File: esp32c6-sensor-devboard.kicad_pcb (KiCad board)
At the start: 4 copper layers, 183 parts, among them J1 Conn_01x04_Pin, J2 Micro_SD_Card_Det1, J3 Screw_Terminal_01x02, J4 USB_C_Receptacle_USB2.0_14P, J5 Screw_Terminal_01x02, J6 Screw_Terminal_01x06, J7 Screw_Terminal_01x04, J8 Conn_01x04_Pin, J9 Conn_01x03_Pin, SW1 SW_Push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

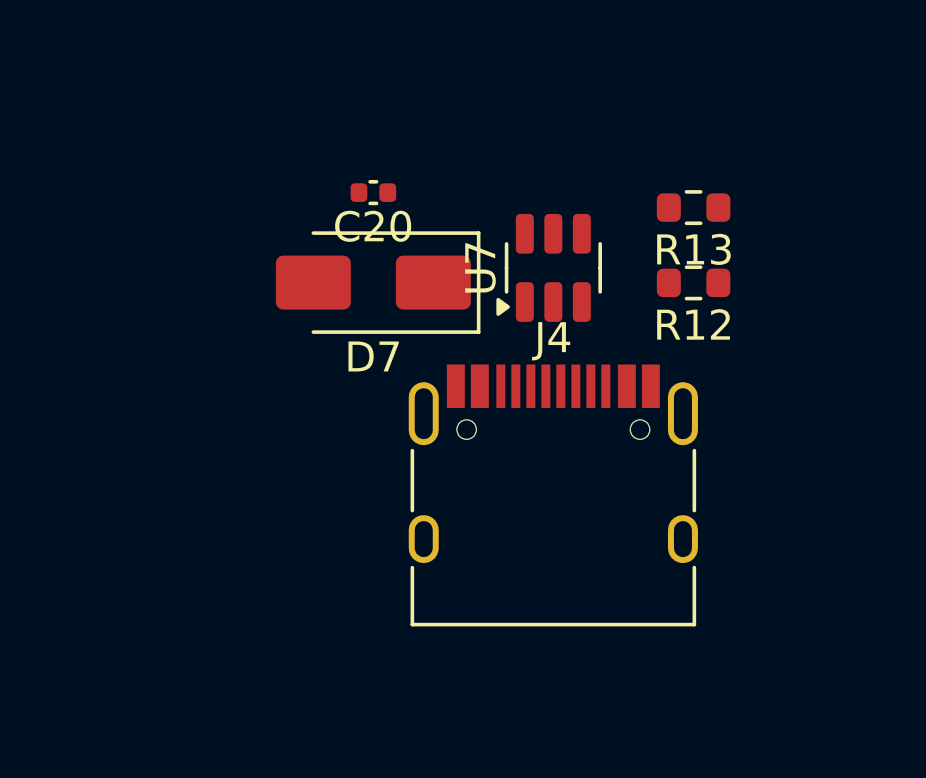
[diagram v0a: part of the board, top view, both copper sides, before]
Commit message: pcb: usb connector layout
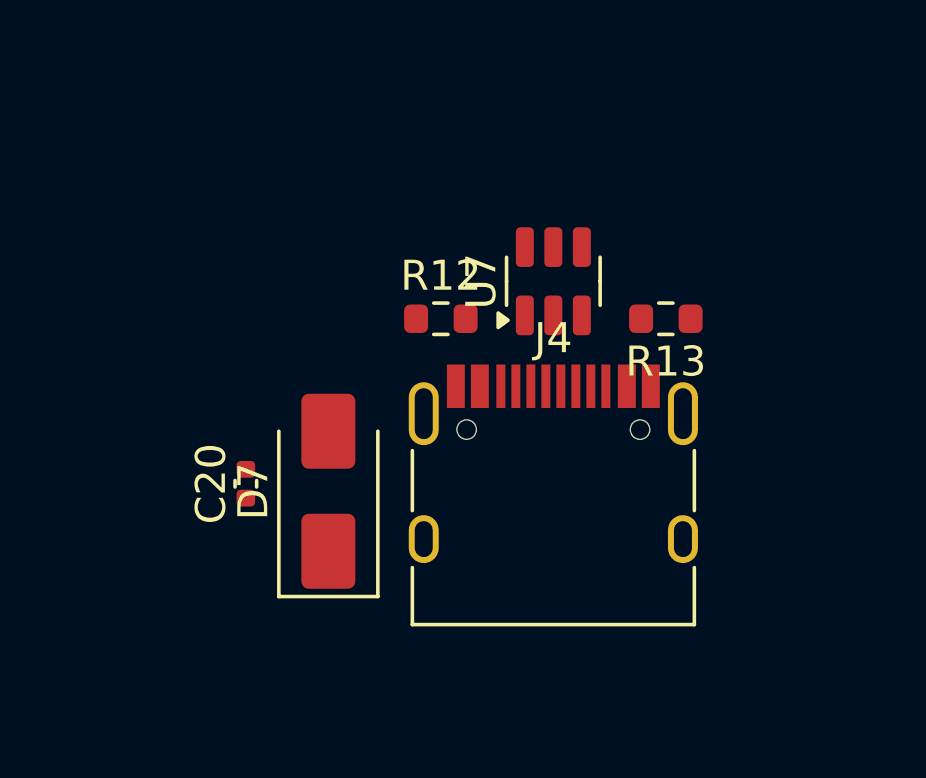
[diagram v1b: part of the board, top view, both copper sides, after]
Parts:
- moved C20 10.6 mm to (140.5, 124.2), turned to 90 degrees
- moved R12 8.51 mm to (147.0, 118.8), turned to 0 degrees
- moved D7 7.11 mm to (143.2, 124.5), turned to 90 degrees
- moved R13 3.82 mm to (154.5, 118.8)
- moved U7 0.44 mm to (150.8, 117.5)

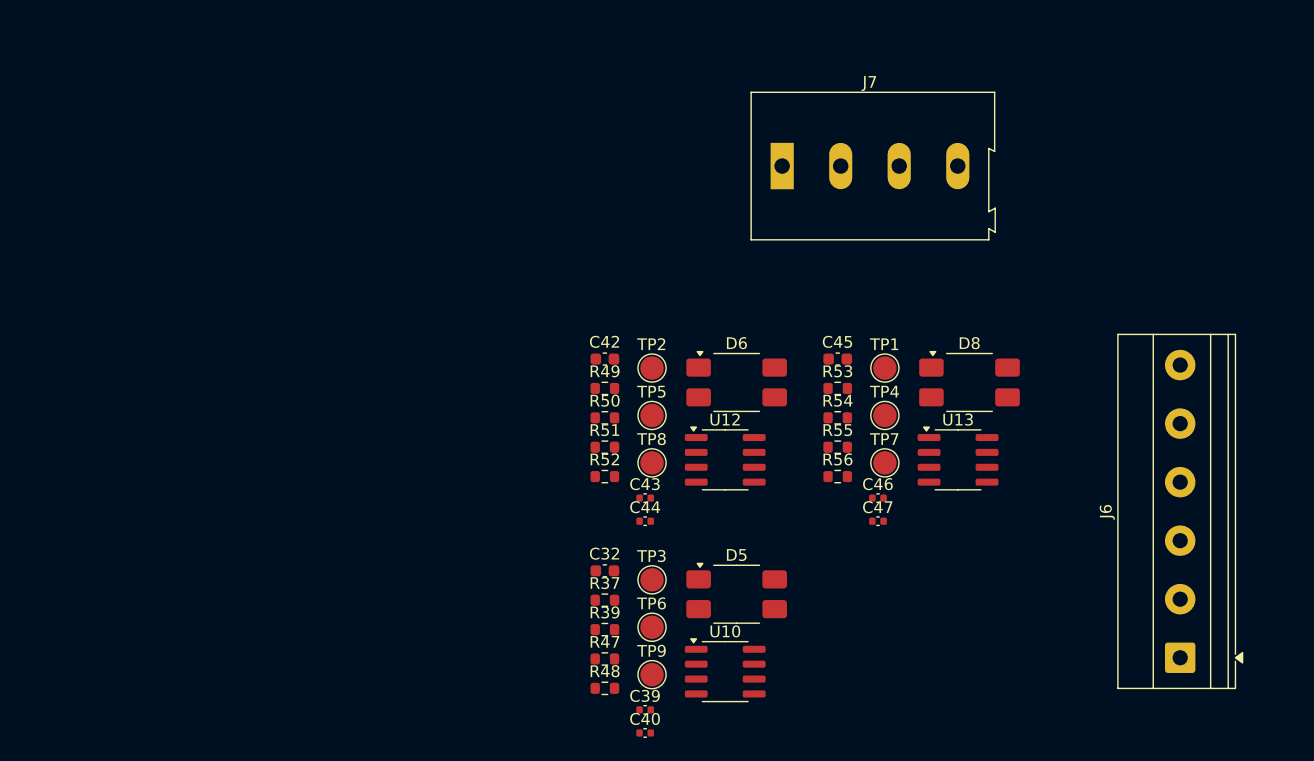
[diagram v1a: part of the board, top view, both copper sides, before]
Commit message: pcb: ac level shifter layout
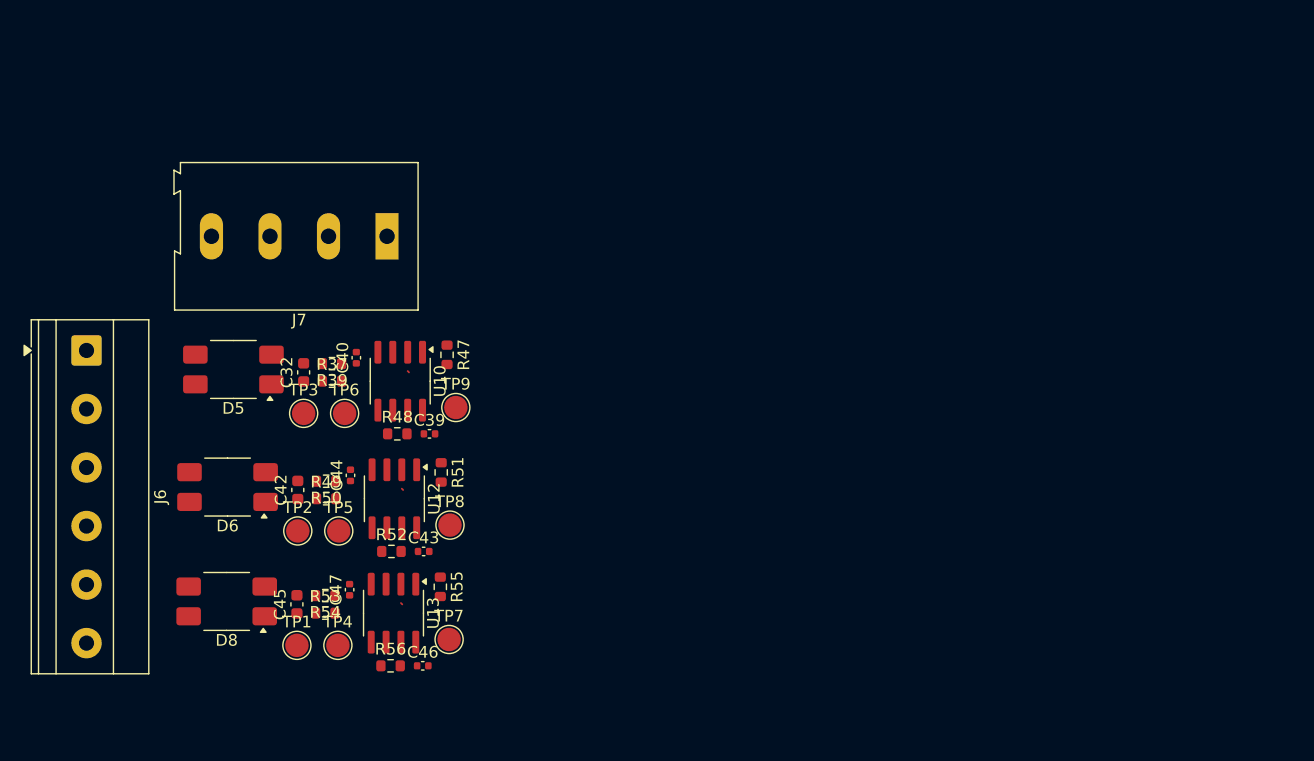
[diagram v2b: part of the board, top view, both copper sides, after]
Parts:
- moved J6 97.0 mm to (19.6, 147.8), turned to -90 degrees
- moved D8 66.1 mm to (31.6, 169.2), turned to 180 degrees
- moved TP1 55.5 mm to (37.5, 172.9)
- moved C45 50.7 mm to (37.5, 169.4), turned to 90 degrees
- moved TP4 50.7 mm to (41.0, 172.9)
- moved U13 50.0 mm to (45.8, 170.2), turned to -90 degrees
- moved R53 47.8 mm to (40.0, 170.2)
- moved D5 47.1 mm to (32.1, 149.4), turned to 180 degrees
- moved R54 46.3 mm to (40.0, 168.7), turned to 180 degrees
- moved C47 45.5 mm to (42.0, 168.2), turned to 90 degrees
- moved D6 44.4 mm to (31.6, 159.4), turned to 180 degrees
- moved R56 41.5 mm to (45.5, 174.7)
- moved C46 41.4 mm to (48.3, 174.7)
- moved C40 40.4 mm to (42.6, 148.4), turned to 90 degrees
- moved TP7 40.2 mm to (50.5, 172.4)
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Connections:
- D5 pad 3: /AC Level Shifter2/I1 -> /AC Level Shifter2/I2
- D5 pad 4: /AC Level Shifter2/I2 -> /AC Level Shifter2/I1
- D6 pad 3: /AC Level Shifter1/I1 -> /AC Level Shifter1/I2
- D6 pad 4: /AC Level Shifter1/I2 -> /AC Level Shifter1/I1
- D8 pad 3: /AC Level Shifter/I1 -> /AC Level Shifter/I2
- D8 pad 4: /AC Level Shifter/I2 -> /AC Level Shifter/I1

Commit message: pcb: rf layout
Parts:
- moved C52 5.26 mm to (138.7, 85.2)
- moved R11 4.83 mm to (141.6, 97.9), turned to -45 degrees
- moved L4 4.61 mm to (145.0, 90.2), turned to -45 degrees
- moved C29 4.37 mm to (143.8, 89.5), turned to -135 degrees
- moved L6 4.26 mm to (135.7, 85.2), turned to 0 degrees
- moved L7 4.25 mm to (137.2, 85.8), turned to 90 degrees
- moved C28 4.12 mm to (145.0, 91.8), turned to 180 degrees
- moved AE1 3.75 mm to (132.2, 85.5)
- moved C27 3.69 mm to (145.0, 98.1), turned to 45 degrees
- moved Y2 3.51 mm to (143.0, 96.5), turned to 135 degrees
- moved C11 2.05 mm to (145.0, 93.2)
- moved C9 1.74 mm to (140.8, 90.3)
- moved C8 1.74 mm to (139.8, 90.2)
- moved C26 1.42 mm to (141.1, 94.6), turned to 45 degrees
- moved C10 0.57 mm to (142.5, 91.8), turned to 180 degrees
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
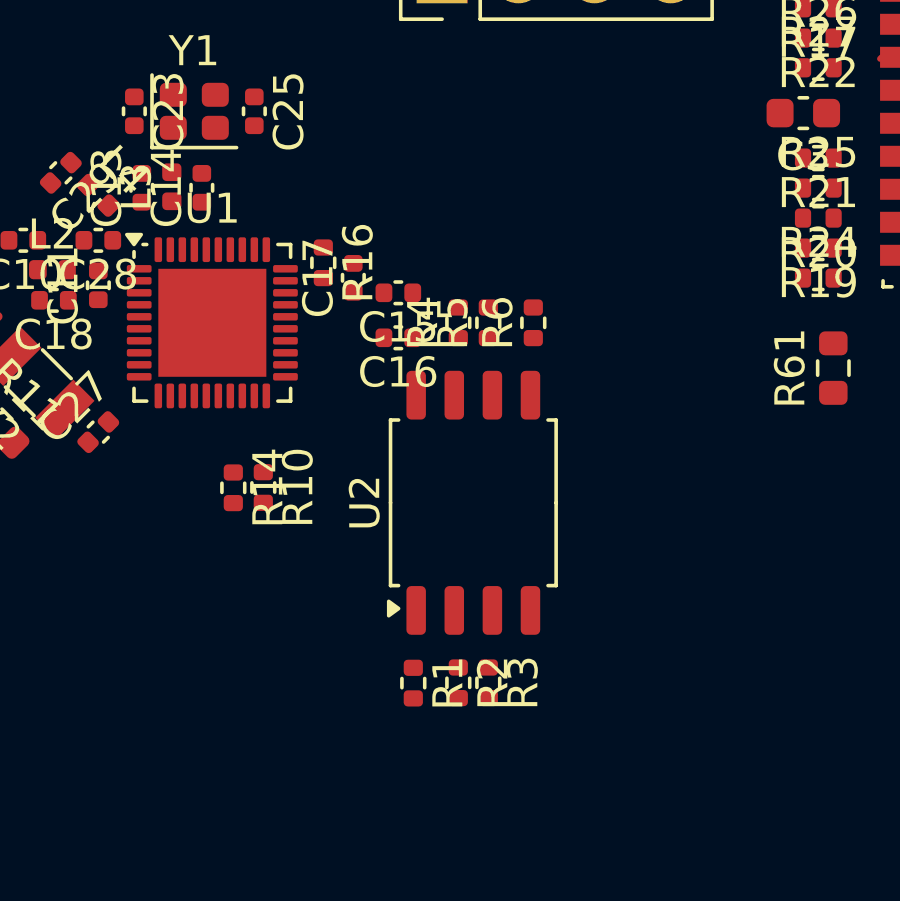
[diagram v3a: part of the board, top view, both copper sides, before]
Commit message: pcb: spi flash layout
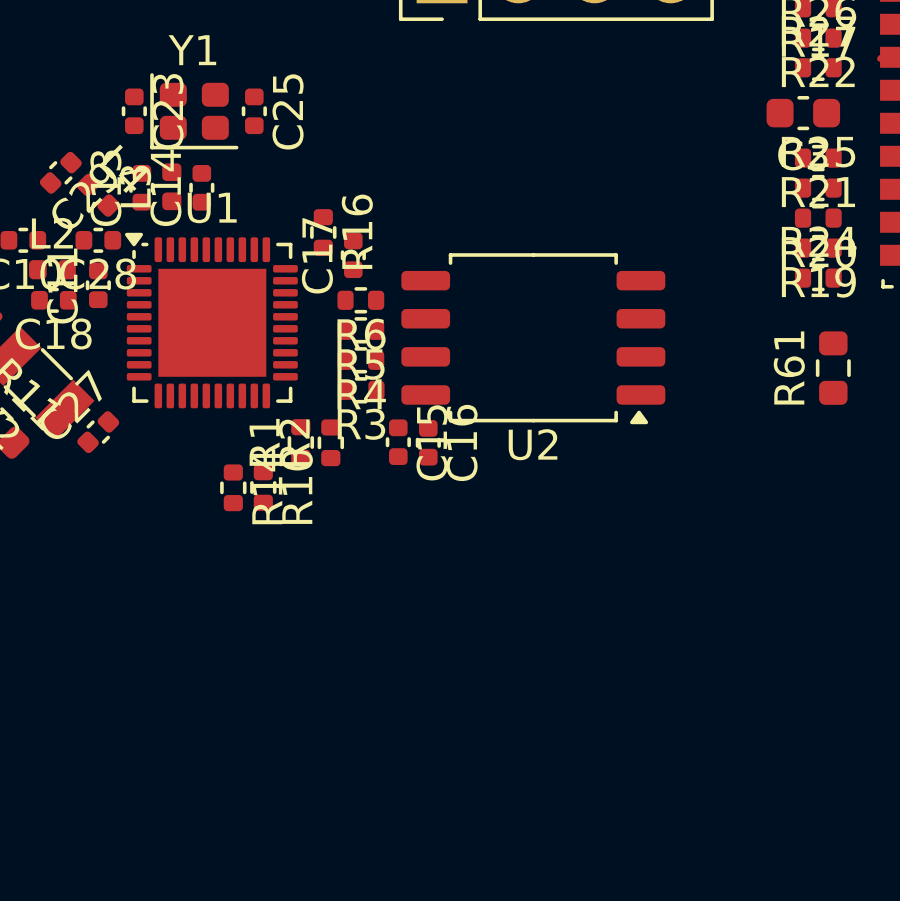
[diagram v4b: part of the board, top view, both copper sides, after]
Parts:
- moved R3 10.6 mm to (153.8, 96.8), turned to 180 degrees
- moved R2 9.06 mm to (152.8, 98.5), turned to 90 degrees
- moved R1 8.85 mm to (151.8, 98.5), turned to 90 degrees
- moved U2 5.85 mm to (159.5, 95.0), turned to 180 degrees
- moved R6 5.80 mm to (153.8, 93.8), turned to 180 degrees
- moved C15 4.98 mm to (155.0, 98.5), turned to -90 degrees
- moved R5 4.26 mm to (153.8, 94.8), turned to 180 degrees
- moved C16 3.64 mm to (156.0, 98.5), turned to -90 degrees
- moved R4 3.48 mm to (153.8, 95.8), turned to 180 degrees
- moved R16 1.01 mm to (152.5, 91.5)
- moved C17 0.75 mm to (153.5, 92.2)

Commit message: pcb: fix 3v3 ldo layout
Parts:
- moved JP3 91.1 mm to (230.0, 26.2), turned to -90 degrees
- moved J1 7.65 mm to (149.9, 79.0)
- moved JP1 7.19 mm to (174.8, 74.5), turned to -90 degrees
- moved C1 3.72 mm to (224.2, 32.8)
- moved C2 3.72 mm to (230.2, 32.2)
- moved D2 3.72 mm to (222.5, 29.5)
- moved R15 3.72 mm to (224.2, 29.5)
- moved TP17 3.72 mm to (227.2, 33.8)
- moved U3 3.72 mm to (227.2, 30.2)
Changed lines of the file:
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@@
 	(footprint "Connector_PinHeader_2.54mm:PinHeader_1x04_P2.54mm_Vertical"
 		(layer "F.Cu")
-		(at 156.46 83 90)
+		(at 149.94 79 90)
 		(descr "Through hole straight pin header, 1x04, 2.54mm pitch, single row")
 		(tags "Through hole pin header THT 1x04 2.54mm single row")
@@
 	(footprint "Capacitor_SMD:C_0603_1608Metric"
 		(layer "F.Cu")
-		(at 223.8625 29.075 -90)
+		(at 224.25 32.775 -90)
 		(descr "Capacitor SMD 0603 (1608 Metric), square (rectangular) end terminal, IPC-7351 nominal, (Body size source: IPC-SM-782 page 76, https://www.pcb-3d.com/wordpress/wp-content/uploads/ipc-sm-782a_amendment_1_and_2.pdf), generated with kicad-footprint-generator")
 		(tags "capacitor")
@@
 	(footprint "Capacitor_SMD:C_0603_1608Metric"
 		(layer "F.Cu")
-		(at 229.8625 28.55 -90)
+		(at 230.25 32.25 -90)
 		(descr "Capacitor SMD 0603 (1608 Metric), square (rectangular) end terminal, IPC-7351 nominal, (Body size source: IPC-SM-782 page 76, https://www.pcb-3d.com/wordpress/wp-content/uploads/ipc-sm-782a_amendment_1_and_2.pdf), generated with kicad-footprint-generator")
 		(tags "capacitor")
@@
 	(footprint "Connector_PinHeader_2.54mm:PinHeader_1x02_P2.54mm_Vertical"
 		(layer "F.Cu")
-		(at 225.49 117.195)
+		(at 230.025 26.25 -90)
 		(descr "Through hole straight pin header, 1x02, 2.54mm pitch, single row")
 		(tags "Through hole pin header THT 1x02 2.54mm single row")
 		(property "Reference" "JP3"
-			(at 0 -2.38 0)
+			(at 0 -2.38 90)
 			(layer "F.SilkS")
 			(effects
@@
 		)
 		(property "Value" "Jumper_2_Bridged"
-			(at 0 4.92 0)
+			(at 0 4.92 90)
 			(layer "F.Fab")
 			(effects
@@
 		)
 		(property "Datasheet" "~"
-			(at 0 0 0)
+			(at 0 0 90)
 			(layer "F.Fab")
 			(hide yes)
@@
 		)
 		(property "Description" "Jumper, 2-pole, closed/bridged"
-			(at 0 0 0)
+			(at 0 0 90)
 			(layer "F.Fab")
 			(hide yes)
@@
 		(attr through_hole exclude_from_bom)
 		(fp_line
-			(start -1.38 -1.38)
-			(end 0 -1.38)
+			(start -1.38 3.92)
+			(end 1.38 3.92)
 			(stroke
 				(width 0.12)
@@
 		)
 		(fp_line
-			(start -1.38 0)
-			(end -1.38 -1.38)
+			(start -1.38 1.27)
+			(end -1.38 3.92)
 			(stroke
 				(width 0.12)
@@
 		(fp_line
 			(start -1.38 1.27)
-			(end -1.38 3.92)
+			(end 1.38 1.27)
 			(stroke
 				(width 0.12)
@@
 		)
 		(fp_line
-			(start -1.38 1.27)
-			(end 1.38 1.27)
+			(start 1.38 1.27)
+			(end 1.38 3.92)
 			(stroke
 				(width 0.12)
@@
 		)
 		(fp_line
-			(start -1.38 3.92)
-			(end 1.38 3.92)
+			(start -1.38 0)
+			(end -1.38 -1.38)
 			(stroke
 				(width 0.12)
@@
 		)
 		(fp_line
-			(start 1.38 1.27)
-			(end 1.38 3.92)
+			(start -1.38 -1.38)
+			(end 0 -1.38)
 			(stroke
 				(width 0.12)
@@
 		)
 		(fp_line
-			(start -1.77 -1.77)
-			(end -1.77 4.32)
+			(start -1.77 4.32)
+			(end 1.77 4.32)
 			(stroke
 				(width 0.05)
@@
 		)
 		(fp_line
-			(start -1.77 4.32)
-			(end 1.77 4.32)
+			(start 1.77 4.32)
+			(end 1.77 -1.77)
 			(stroke
 				(width 0.05)
@@
 		)
 		(fp_line
-			(start 1.77 -1.77)
-			(end -1.77 -1.77)
+			(start -1.77 -1.77)
+			(end -1.77 4.32)
 			(stroke
 				(width 0.05)
@@
 		)
 		(fp_line
-			(start 1.77 4.32)
-			(end 1.77 -1.77)
+			(start 1.77 -1.77)
+			(end -1.77 -1.77)
 			(stroke
 				(width 0.05)
@@
 		)
 		(fp_line
-			(start -1.27 -0.635)
-			(end -0.635 -1.27)
+			(start -1.27 3.81)
+			(end -1.27 -0.635)
 			(stroke
 				(width 0.1)
@@
 		)
 		(fp_line
-			(start -1.27 3.81)
-			(end -1.27 -0.635)
+			(start 1.27 3.81)
+			(end -1.27 3.81)
 			(stroke
 				(width 0.1)
@@
 		)
 		(fp_line
-			(start -0.635 -1.27)
-			(end 1.27 -1.27)
+			(start -1.27 -0.635)
+			(end -0.635 -1.27)
 			(stroke
 				(width 0.1)
@@
 		)
 		(fp_line
-			(start 1.27 -1.27)
-			(end 1.27 3.81)
+			(start -0.635 -1.27)
+			(end 1.27 -1.27)
 			(stroke
 				(width 0.1)
@@
 		)
 		(fp_line
-			(start 1.27 3.81)
-			(end -1.27 3.81)
+			(start 1.27 -1.27)
+			(end 1.27 3.81)
 			(stroke
 				(width 0.1)
@@
 		)
 		(fp_text user "${REFERENCE}"
-			(at 0 1.27 90)
+			(at 0 1.27 0)
 			(layer "F.Fab")
 			(effects
@@
 		)
 		(pad "1" thru_hole rect
-			(at 0 0)
+			(at 0 0 270)
 			(size 1.7 1.7)
 			(drill 1)
@@
 		)
 		(pad "2" thru_hole circle
-			(at 0 2.54)
+			(at 0 2.54 270)
 			(size 1.7 1.7)
 			(drill 1)
@@
 	(footprint "Package_TO_SOT_SMD:SOT-23-5"
 		(layer "F.Cu")
-		(at 226.8625 26.55 180)
+		(at 227.25 30.25 180)
 		(descr "SOT, 5 Pin (JEDEC MO-178 Var AA https://www.jedec.org/document_search?search_api_views_fulltext=MO-178), generated with kicad-footprint-generator ipc_gullwing_generator.py")
 		(tags "SOT TO_SOT_SMD")
@@
 	(footprint "Connector_PinHeader_2.54mm:PinHeader_1x02_P2.54mm_Vertical"
 		(layer "F.Cu")
-		(at 181.8975 73.68 90)
+		(at 174.75 74.5 -90)
 		(descr "Through hole straight pin header, 1x02, 2.54mm pitch, single row")
 		(tags "Through hole pin header THT 1x02 2.54mm single row")
@@
 		(attr through_hole exclude_from_bom)
 		(fp_line
-			(start -1.38 -1.38)
-			(end 0 -1.38)
+			(start -1.38 3.92)
+			(end 1.38 3.92)
 			(stroke
 				(width 0.12)
@@
 		)
 		(fp_line
-			(start -1.38 0)
-			(end -1.38 -1.38)
+			(start -1.38 1.27)
+			(end -1.38 3.92)
 			(stroke
 				(width 0.12)
@@
 		)
 		(fp_line
-			(start 1.38 1.27)
-			(end 1.38 3.92)
+			(start -1.38 1.27)
+			(end 1.38 1.27)
 			(stroke
 				(width 0.12)
@@
 		)
 		(fp_line
-			(start -1.38 1.27)
-			(end 1.38 1.27)
+			(start 1.38 1.27)
+			(end 1.38 3.92)
 			(stroke
 				(width 0.12)
@@
 		)
 		(fp_line
-			(start -1.38 1.27)
-			(end -1.38 3.92)
+			(start -1.38 0)
+			(end -1.38 -1.38)
 			(stroke
 				(width 0.12)
@@
 		)
 		(fp_line
-			(start -1.38 3.92)
-			(end 1.38 3.92)
+			(start -1.38 -1.38)
+			(end 0 -1.38)
 			(stroke
 				(width 0.12)
@@
 		)
 		(fp_line
-			(start 1.77 -1.77)
-			(end -1.77 -1.77)
+			(start -1.77 4.32)
+			(end 1.77 4.32)
 			(stroke
 				(width 0.05)
@@
 		)
 		(fp_line
-			(start -1.77 -1.77)
-			(end -1.77 4.32)
+			(start 1.77 4.32)
+			(end 1.77 -1.77)
 			(stroke
 				(width 0.05)
@@
 		)
 		(fp_line
-			(start 1.77 4.32)
-			(end 1.77 -1.77)
+			(start -1.77 -1.77)
+			(end -1.77 4.32)
 			(stroke
 				(width 0.05)
@@
 		)
 		(fp_line
-			(start -1.77 4.32)
-			(end 1.77 4.32)
+			(start 1.77 -1.77)
+			(end -1.77 -1.77)
 			(stroke
 				(width 0.05)
@@
 		)
 		(fp_line
-			(start 1.27 -1.27)
-			(end 1.27 3.81)
+			(start -1.27 3.81)
+			(end -1.27 -0.635)
 			(stroke
 				(width 0.1)
@@
 		)
 		(fp_line
-			(start -0.635 -1.27)
-			(end 1.27 -1.27)
+			(start 1.27 3.81)
+			(end -1.27 3.81)
 			(stroke
 				(width 0.1)
@@
 		)
 		(fp_line
-			(start 1.27 3.81)
-			(end -1.27 3.81)
+			(start -0.635 -1.27)
+			(end 1.27 -1.27)
 			(stroke
 				(width 0.1)
@@
 		)
 		(fp_line
-			(start -1.27 3.81)
-			(end -1.27 -0.635)
+			(start 1.27 -1.27)
+			(end 1.27 3.81)
 			(stroke
 				(width 0.1)
@@
 		)
 		(pad "1" thru_hole rect
-			(at 0 0 90)
+			(at 0 0 270)
 			(size 1.7 1.7)
 			(drill 1)
@@
 		)
 		(pad "2" thru_hole circle
-			(at 0 2.54 90)
+			(at 0 2.54 270)
 			(size 1.7 1.7)
 			(drill 1)
@@
 	(footprint "LED_SMD:LED_0805_2012Metric"
 		(layer "F.Cu")
-		(at 222.1125 25.825 90)
+		(at 222.5 29.525 90)
 		(descr "LED SMD 0805 (2012 Metric), square (rectangular) end terminal, IPC-7351 nominal, (Body size source: https://docs.google.com/spreadsheets/d/1BsfQQcO9C6DZCsRaXUlFlo91Tg2WpOkGARC1WS5S8t0/edit?usp=sharing), generated with kicad-footprint-generator")
 		(tags "LED")
@@
 	(footprint "Resistor_SMD:R_0603_1608Metric"
 		(layer "F.Cu")
-		(at 223.8625 25.825 90)
+		(at 224.25 29.525 90)
 		(descr "Resistor SMD 0603 (1608 Metric), square (rectangular) end terminal, IPC-7351 nominal, (Body size source: IPC-SM-782 page 72, https://www.pcb-3d.com/wordpress/wp-content/uploads/ipc-sm-782a_amendment_1_and_2.pdf), generated with kicad-footprint-generator")
 		(tags "resistor")
@@
 	(footprint "TestPoint:TestPoint_Pad_D2.0mm"
 		(layer "F.Cu")
-		(at 226.8625 30.05)
+		(at 227.25 33.75)
 		(descr "SMD pad as test Point, diameter 2.0mm")
 		(tags "test point SMD pad")
